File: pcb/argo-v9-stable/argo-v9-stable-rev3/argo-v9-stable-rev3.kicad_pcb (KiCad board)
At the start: 2 copper layers, 94.8 x 67.2 mm, 102 parts, among them IC1 MP2672GD, J1 Sparkfun_NEO-N9M-SMA, J2 USB4125-GF-A, J3 LED_power_button_RGB_LED, J4 Conn_I2C_Molex_705450003, J5 Conn_I2C_Molex_705450003, K1 PRL3-5V-DC-1A, Q1 BSD840N, Q2 BSD840N, SW1 POW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

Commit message: **** Argo PCB rev3 sent for JLCPCB fabrication - 3d models for GPS and LORA daughterboards - improved cable connections and i2c headers - many circuit fixes to fix problems with rev2 PCB - improved overvoltage diode protection for FETs and OPi pins - fixed i2c buffer connections - improved power routing - adjusted many R values to be correct - fixed LORA pins and place LORA daughterboard on PCB - moved BNO085 to i2c connector for mounting away from power relay - many additional scope probe test points
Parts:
- added TP7: 5V, Argo footprint Library:TestPoint_scope_probe_autonamed, F.Cu at (67.8, 88.7)
- C6: value 1u25V -> 1u 25V
- J1: footprint sparkfun:Sparkfun_NEO-M9N-SMA-scaled -> Argo footprint Library:Sparkfun_NEO-M9N-SMA
- J3: footprint Argo footprint Library:JST_XH_B6B-XH-AM_1x06_P2.50mm_Vertical -> Argo footprint Library:JST_XH_S6B-XH-A_1x06_P2.50mm_Horizontal
- moved U6 15.3 mm to (138.2, 73.9), turned to 180 degrees
- moved R16 10.9 mm to (126.5, 80.7)
- moved R25 10.9 mm to (126.5, 77.2)
- moved SW1 10.8 mm to (123.6, 92.7)
- moved D1 9.76 mm to (128.4, 80.7)
- moved R1 9.20 mm to (138.3, 30.4)
- moved R34 7.70 mm to (137.1, 56.4), turned to -90 degrees
- moved C1 6.54 mm to (138.3, 33.7), turned to 90 degrees
- moved R_{CC2}1 6.53 mm to (141.6, 90.0), turned to 90 degrees
- moved J3 5.82 mm to (142.1, 53.2)
- moved R23 4.42 mm to (138.1, 46.4)
- moved Q1 3.80 mm to (136.2, 53.1)
- moved R_{CC1}1 1.30 mm to (139.8, 90.0)
- moved Q2 0.68 mm to (116.3, 93.0)
- moved F2 0.57 mm to (133.2, 79.1)
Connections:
- J3 pad 2: /POW_BUT -> /POW_ON
- POW_BUT1 pad 2: /POW_BUT -> /POW_ON
- Q2 pad 2: /POW_BUT -> /POW_ON
- R25 pad 2: /POW_BUT -> /POW_ON
- SW1 pad 2: /POW_BUT -> /POW_ON
- TP6 pad 1: /POW_BUT -> /POW_ON
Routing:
- net /POW_ON: track 0.00 -> 95.4 mm, vias 0 -> 7
- net /POW_BUT: track 190.2 -> 117.9 mm, vias 9 -> 13
- net /SPI_SCLK: track 85.6 -> 124.6 mm, vias 8 -> 11
- net /MOSI: track 87.5 -> 111.7 mm, vias 4 -> 7
- net /!LORA_RST: track 86.7 -> 108.8 mm, vias 3 -> 7
- net /MISO: track 87.0 -> 106.2 mm, vias 2 -> 5
- net /SCK: track 142.6 -> 123.8 mm, vias 10 -> 7
- net /PSR: track 131.4 -> 114.4 mm, vias 5 -> 6
- net /FUSE: track 144.5 -> 160.1 mm, vias 5 -> 8
- net /LORA_OUT: track 97.5 -> 112.0 mm, vias 4 -> 6
- net /!LORA_SEL: track 93.8 -> 105.8 mm, vias 6 -> 5
- net +3.3V: track 156.9 -> 166.9 mm
- net /SALTWATER: track 110.6 -> 119.4 mm, vias 4 -> 5
- net GND: track 729.4 -> 724.0 mm
- net /BLUE: track 117.6 -> 112.4 mm
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
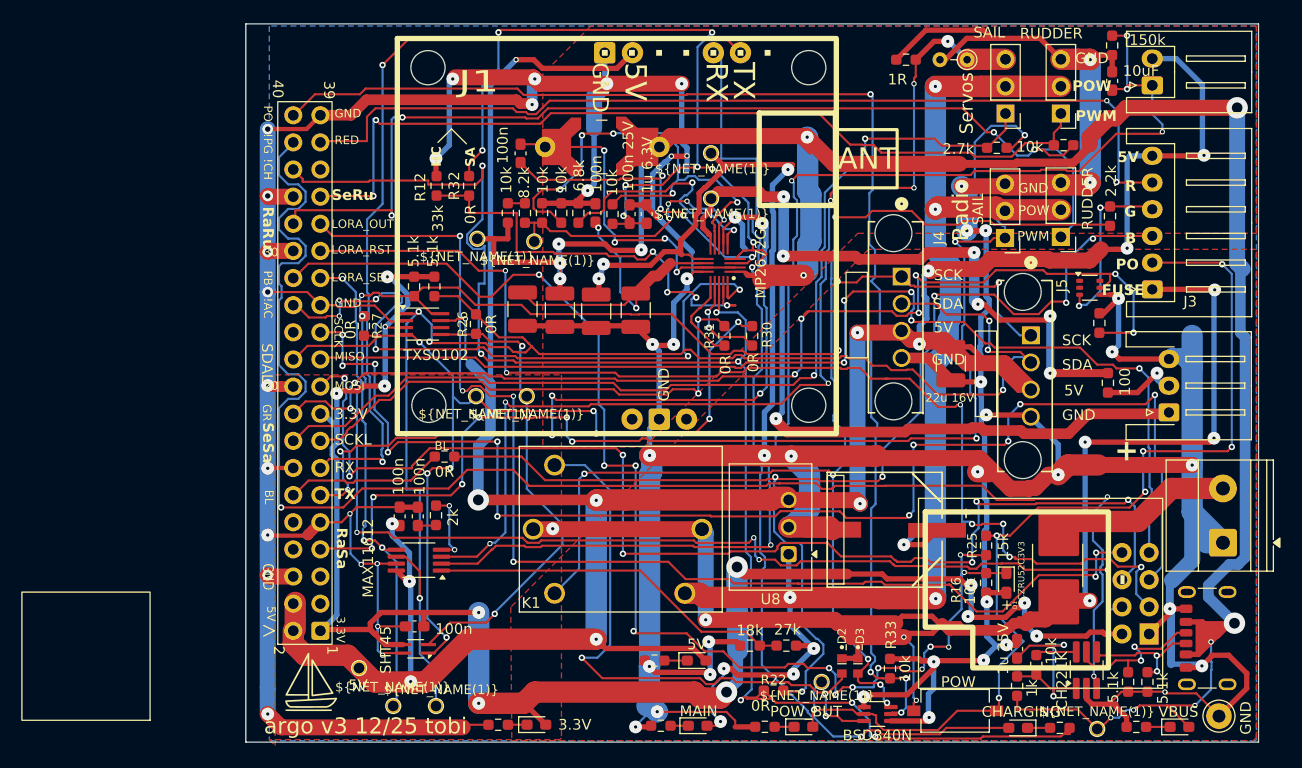
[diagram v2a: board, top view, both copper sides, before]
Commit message: argo pcb updates after fab to make things better like visible silkscreen and componet imperovmeents
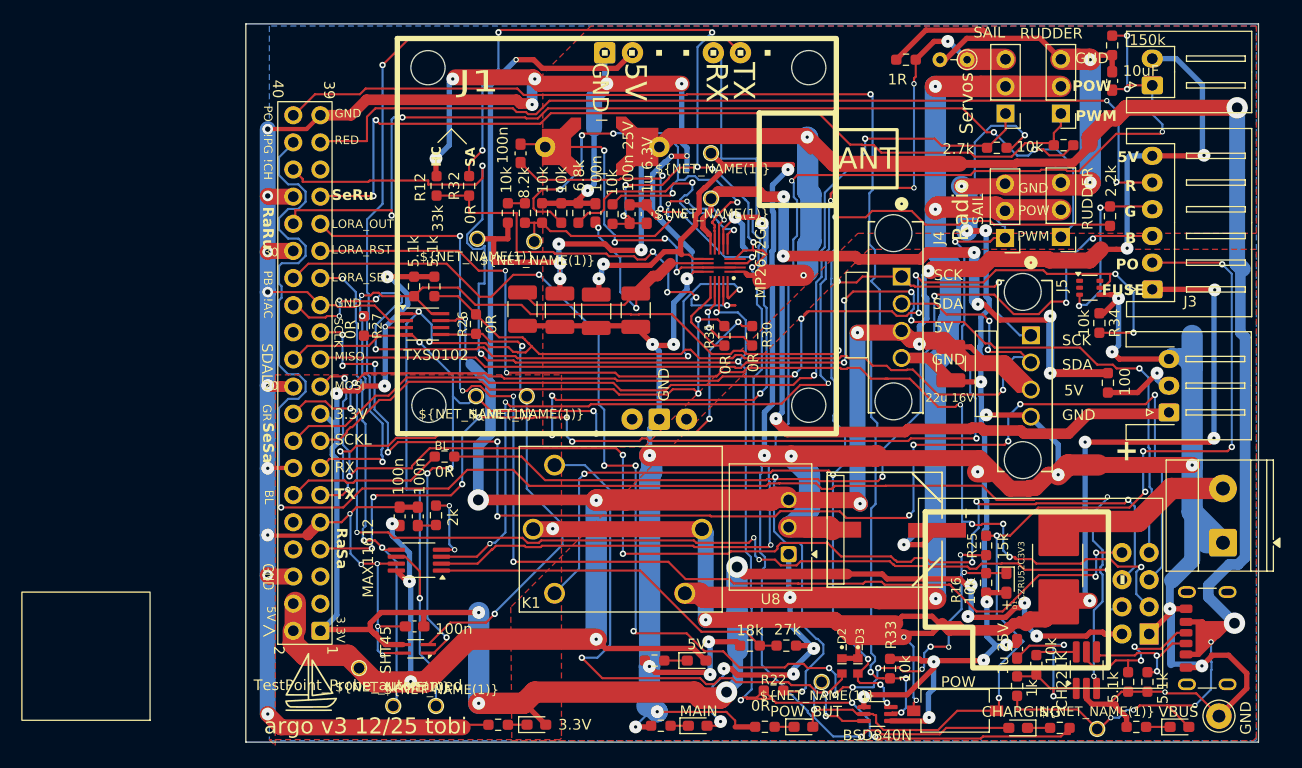
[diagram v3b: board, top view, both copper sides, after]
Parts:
- TP7: value 5V -> TestPoint_Probe_autonamed
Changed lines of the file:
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@@
 		(sheetname "/")
 		(sheetfile "argo-v9-stable-rev3.kicad_sch")
-		(attr exclude_from_pos_files)
+		(attr exclude_from_pos_files exclude_from_bom)
 		(fp_circle
 			(center 0 0)
@@
 		(sheetname "/")
 		(sheetfile "argo-v9-stable-rev3.kicad_sch")
-		(attr exclude_from_pos_files)
+		(attr exclude_from_pos_files exclude_from_bom)
 		(fp_circle
 			(center 0 0)
@@
 		(sheetname "/")
 		(sheetfile "argo-v9-stable-rev3.kicad_sch")
-		(attr smd)
+		(attr smd dnp)
 		(fp_line
 			(start -0.254724 -0.5225)
@@
 		(sheetname "/")
 		(sheetfile "argo-v9-stable-rev3.kicad_sch")
-		(attr exclude_from_pos_files)
+		(attr exclude_from_pos_files exclude_from_bom)
 		(fp_circle
 			(center 0 0)
@@
 			(at 0 -1.43 90)
 			(layer "F.SilkS")
-			(hide yes)
 			(effects
 				(font
@@
 		(property "Value" "10k"
 			(at 0 1.43 90)
-			(layer "F.Fab")
+			(layer "F.SilkS")
 			(effects
 				(font
@@
 		(sheetname "/")
 		(sheetfile "argo-v9-stable-rev3.kicad_sch")
-		(attr exclude_from_pos_files)
+		(attr exclude_from_pos_files exclude_from_bom)
 		(fp_circle
 			(center 0 0)
@@
 		(sheetname "/")
 		(sheetfile "argo-v9-stable-rev3.kicad_sch")
-		(attr exclude_from_pos_files)
+		(attr exclude_from_pos_files exclude_from_bom)
 		(fp_circle
 			(center 0 0)
@@
 		(sheetname "/")
 		(sheetfile "argo-v9-stable-rev3.kicad_sch")
-		(attr smd)
+		(attr smd dnp)
 		(fp_line
 			(start -0.254724 -0.5225)
@@
 		(sheetname "/")
 		(sheetfile "argo-v9-stable-rev3.kicad_sch")
-		(attr exclude_from_pos_files)
+		(attr exclude_from_pos_files exclude_from_bom)
 		(fp_circle
 			(center 0 0)
@@
 		(sheetname "/")
 		(sheetfile "argo-v9-stable-rev3.kicad_sch")
-		(attr through_hole)
+		(attr through_hole dnp)
 		(fp_line
 			(start 0.92 0)
@@
 		(sheetname "/")
 		(sheetfile "argo-v9-stable-rev3.kicad_sch")
-		(attr smd)
+		(attr smd dnp)
 		(fp_line
 			(start -0.254724 -0.5225)
@@
 		(sheetname "/")
 		(sheetfile "argo-v9-stable-rev3.kicad_sch")
-		(attr exclude_from_pos_files)
+		(attr exclude_from_pos_files exclude_from_bom)
 		(fp_circle
 			(center 0 0)
@@
 			)
 		)
-		(property "Value" "5V"
+		(property "Value" "TestPoint_Probe_autonamed"
 			(at -0.1 1.6 0)
 			(layer "F.SilkS")
@@
 		(sheetname "/")
 		(sheetfile "argo-v9-stable-rev3.kicad_sch")
-		(attr exclude_from_pos_files)
+		(attr exclude_from_pos_files exclude_from_bom)
 		(fp_circle
 			(center 0 0)
@@
 		(sheetname "/")
 		(sheetfile "argo-v9-stable-rev3.kicad_sch")
-		(attr smd)
+		(attr smd dnp)
 		(fp_line
 			(start -0.254724 -0.5225)
@@
 		(sheetname "/")
 		(sheetfile "argo-v9-stable-rev3.kicad_sch")
-		(attr exclude_from_pos_files)
+		(attr exclude_from_pos_files exclude_from_bom)
 		(fp_circle
 			(center 0 0)
@@
 		(sheetname "/")
 		(sheetfile "argo-v9-stable-rev3.kicad_sch")
-		(attr exclude_from_pos_files)
+		(attr exclude_from_pos_files exclude_from_bom)
 		(fp_circle
 			(center 0 0)
@@
 		(sheetname "/")
 		(sheetfile "argo-v9-stable-rev3.kicad_sch")
-		(attr smd)
+		(attr smd dnp)
 		(fp_line
 			(start -0.254724 -0.5225)
@@
 		(sheetname "/")
 		(sheetfile "argo-v9-stable-rev3.kicad_sch")
-		(attr smd)
+		(attr smd dnp)
 		(fp_line
 			(start -0.254724 -0.5225)
@@
 		(sheetname "/")
 		(sheetfile "argo-v9-stable-rev3.kicad_sch")
-		(attr exclude_from_pos_files)
+		(attr exclude_from_pos_files exclude_from_bom)
 		(fp_circle
 			(center 0 0)
@@
 		(sheetname "/")
 		(sheetfile "argo-v9-stable-rev3.kicad_sch")
-		(attr smd)
+		(attr smd dnp)
 		(fp_line
 			(start -0.254724 -0.5225)
